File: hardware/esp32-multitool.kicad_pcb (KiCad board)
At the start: 4 copper layers, 90.4 x 58.4 mm, 68 parts, among them J1 Conn_01x03/1Wire, J2 Conn_01x04/QWiiC, J3 Conn_01x04/QWiiC, J4 Conn_01x02/VIN, J5 Conn_01x04/VIN_PROTECTED, J6 Conn_01x02/DIN, J7 Conn_01x02/AIN, J8 Conn_01x02/PWM, Q2 AO3400A, U2 mini_esp32, U3 LM393, U9 AOZ1280CI

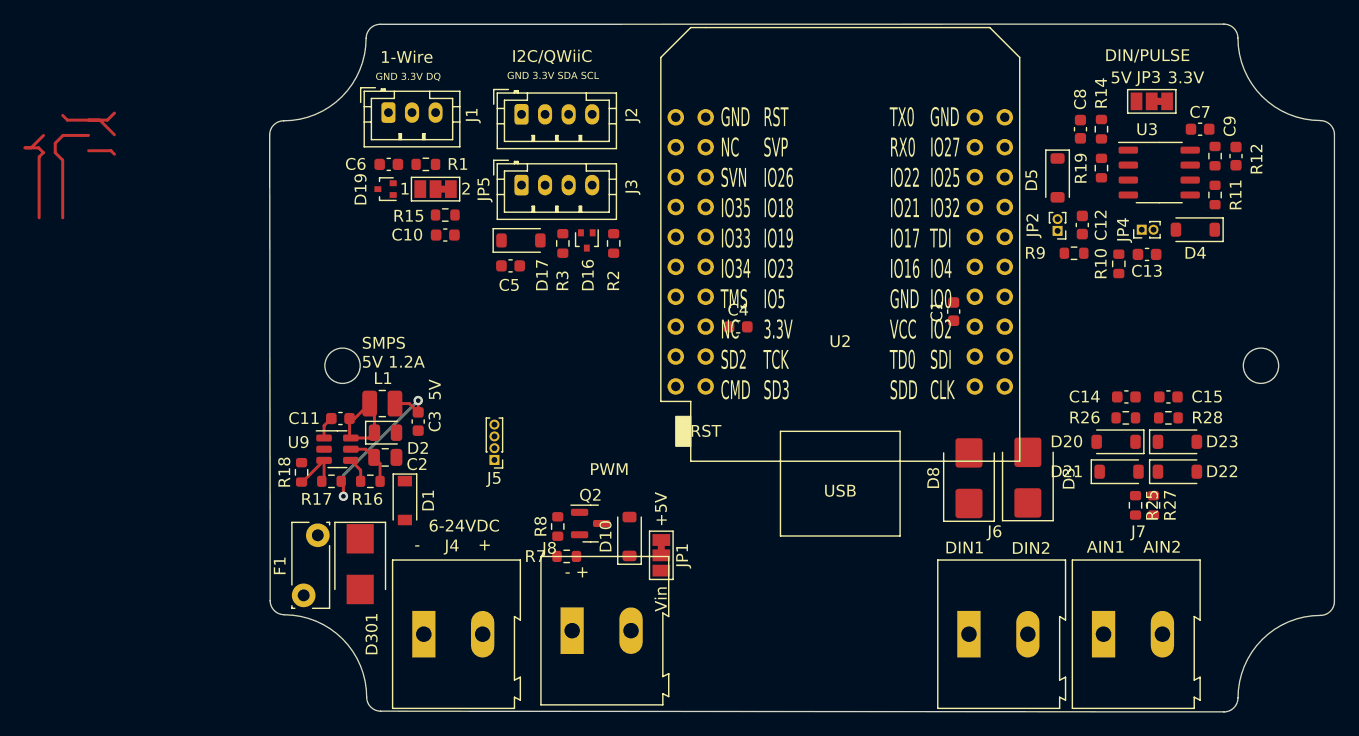
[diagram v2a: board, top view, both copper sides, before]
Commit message: Added 3D models and ran freerouting
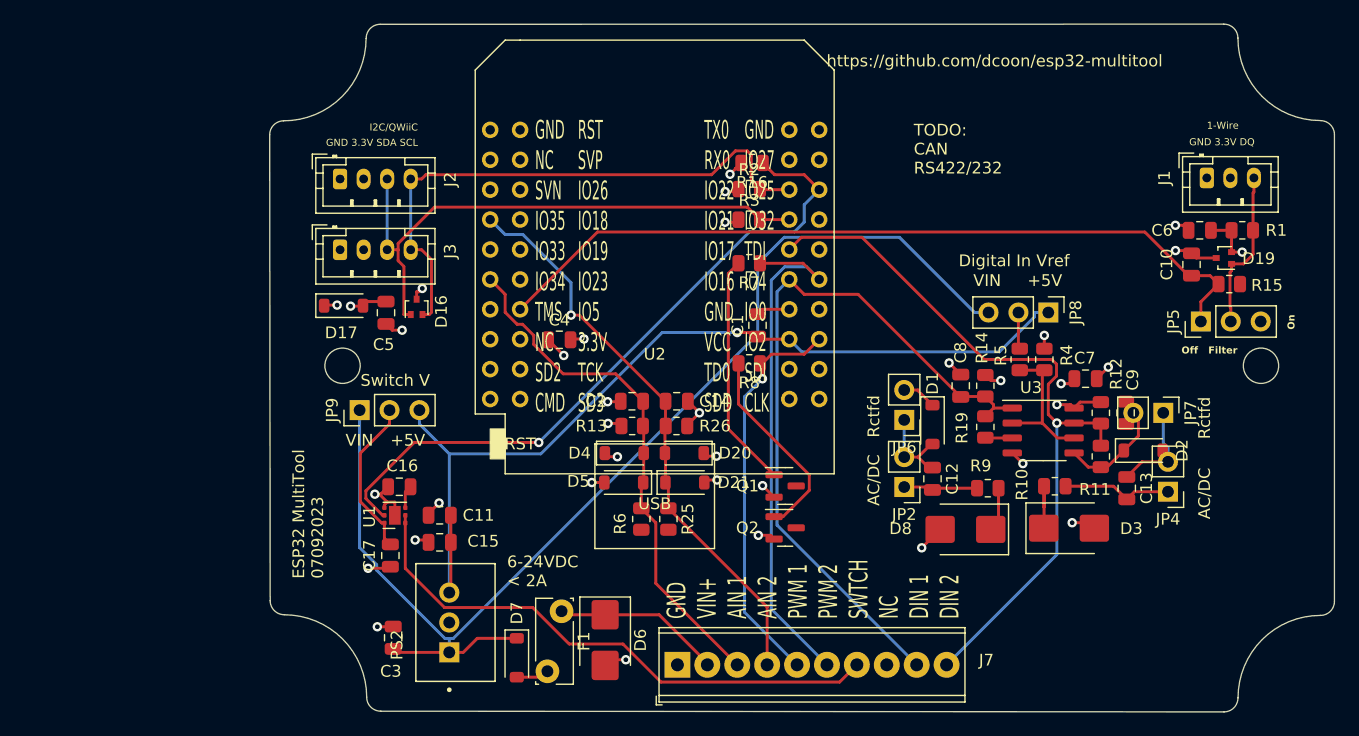
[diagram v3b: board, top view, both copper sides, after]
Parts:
- removed D10, D22, D23: D_SCHOTTKY_30V, Diode_SMD:D_SOD-123
- removed D301: D_TVS_30V, Diode_SMD:D_SMB
- removed J4: Conn_01x02/VIN, TerminalBlock:TerminalBlock_Altech_AK300-2_P5.00mm
- removed J5: Conn_01x04/VIN_PROTECTED, Connector_PinHeader_1.00mm:PinHeader_1x04_P1.00mm_Vertical
- removed J6: Conn_01x02/DIN, TerminalBlock:TerminalBlock_Altech_AK300-2_P5.00mm
- removed J8: Conn_01x02/PWM, TerminalBlock:TerminalBlock_Altech_AK300-2_P5.00mm
- removed JP1, JP3: SolderJumper_3_Bridged12, Jumper:SolderJumper-3_P1.3mm_Bridged12_Pad1.0x1.5mm_NumberLabels
- removed L1: 2.2uH, Inductor_SMD:L_1008_2520Metric
- removed R17: 49.9k, Resistor_SMD:R_0603_1608Metric
- removed R18: 9.53k, Resistor_SMD:R_0603_1608Metric
- removed R27: 100k, Resistor_SMD:R_0603_1608Metric
- removed R28: 1M, Resistor_SMD:R_0603_1608Metric
- removed U9: AOZ1280CI, Package_TO_SOT_SMD:SOT-23-6
- added C16: 4700p, Capacitor_SMD:C_0805_2012Metric, F.Cu at (99.8, 96.1)
- added C17: 4.7uF/30V, Capacitor_SMD:C_0805_2012Metric, F.Cu at (99.1, 101.9)
- added D6: D_TVS_30V, Diode_SMD:D_SMB, F.Cu at (117.3, 109.1)
- added D7: D_SCHOTTKY_30V, Diode_SMD:D_SOD-123, F.Cu at (109.8, 110.6)
- added JP6: Jumper_2_Bridged, Connector_PinHeader_2.54mm:PinHeader_1x02_P2.54mm_Vertical, F.Cu at (142.7, 90.4)
- added JP7: Jumper_2_Bridged, Connector_PinHeader_2.54mm:PinHeader_1x02_P2.54mm_Vertical, F.Cu at (164.7, 89.8)
- added JP8: Jumper_2_Open, Connector_PinHeader_2.54mm:PinHeader_1x03_P2.54mm_Vertical, F.Cu at (154.9, 81.3)
- added JP9: Jumper_3_Bridged12, Connector_PinHeader_2.54mm:PinHeader_1x03_P2.54mm_Vertical, F.Cu at (96.4, 89.6)
- added PS2: TPSM84205EAB, TPSM84205EAB:TPSM84205EAB, F.Cu at (104.1, 107.6)
- added Q1: AO3400A, Package_TO_SOT_SMD:SOT-23, F.Cu at (132.6, 96.0)
- added R13: 1M, Resistor_SMD:R_0805_2012Metric, F.Cu at (119.6, 90.9)
- added R4: 10k, Resistor_SMD:R_0805_2012Metric, F.Cu at (152.5, 85.3)
- added R5: 10k, Resistor_SMD:R_0805_2012Metric, F.Cu at (154.6, 85.3)
- added R6: 100k, Resistor_SMD:R_0805_2012Metric, F.Cu at (120.4, 98.8)
- added U1: TPS22810DRV, Package_SON:WSON-6-1EP_2x2mm_P0.65mm_EP1x1.6mm, F.Cu at (99.4, 98.5)
- C1, C10, C12, C13, C14, C4, C5, C6, C7, C8, C9: footprint Capacitor_SMD:C_0603_1608Metric -> Capacitor_SMD:C_0805_2012Metric
- C11: value 10nF -> 47uF/16V; footprint Capacitor_SMD:C_0603_1608Metric -> Capacitor_SMD:C_0805_2012Metric
- C15: value 1uF -> 47uF/16V; footprint Capacitor_SMD:C_0603_1608Metric -> Capacitor_SMD:C_0805_2012Metric
- C2: value 4.7uF/30V -> 1uF
- C3: value 10uF -> 10uF/50V; footprint Capacitor_SMD:C_0603_1608Metric -> Capacitor_SMD:C_0805_2012Metric
- D2: value D_SMPS -> D_SCHOTTKY_30V; footprint Diode_SMD:D_0805_2012Metric -> Diode_SMD:D_SOD-123
- J7: value Conn_01x02/AIN -> Conn_01x09; footprint TerminalBlock:TerminalBlock_Altech_AK300-2_P5.00mm -> TerminalBlock_Phoenix:TerminalBlock_Phoenix_MPT-0,5-10-2.54_1x10_P2.54mm_Horizontal
- JP2, JP4: footprint Connector_PinHeader_1.00mm:PinHeader_1x02_P1.00mm_Vertical -> Connector_PinHeader_2.54mm:PinHeader_1x02_P2.54mm_Vertical
- JP5: value SolderJumper_3_Bridged12 -> Jumper_3_Bridged12; footprint Jumper:SolderJumper-3_P1.3mm_Bridged12_Pad1.0x1.5mm_NumberLabels -> Connector_PinHeader_2.54mm:PinHeader_1x03_P2.54mm_Vertical
- R1, R10, R11, R12, R14, R15, R19, R2, R25, R26, R3, R8, R9: footprint Resistor_SMD:R_0603_1608Metric -> Resistor_SMD:R_0805_2012Metric
- R16: value R10k -> 10k/30V; footprint Resistor_SMD:R_0603_1608Metric -> Resistor_SMD:R_0805_2012Metric
- R7: value 10k -> 100; footprint Resistor_SMD:R_0603_1608Metric -> Resistor_SMD:R_0805_2012Metric
- U2: value mini_esp32 -> wemos_mini_esp32
- moved D19 71.4 mm to (169.8, 76.7)
- moved J1 69.7 mm to (168.4, 69.8)
- moved R1 69.6 mm to (171.4, 74.3)
- moved C6 69.1 mm to (167.8, 74.3)
- moved R15 66.8 mm to (170.3, 78.9), turned to 0 degrees
- moved JP5 66.0 mm to (167.9, 82.0), turned to 90 degrees
- moved D2 64.4 mm to (163.0, 93.0)
- moved C10 63.4 mm to (167.1, 77.2), turned to 90 degrees
- moved C15 63.1 mm to (103.2, 100.8), turned to 180 degrees
- moved D4 52.1 mm to (118.9, 93.2), turned to 0 degrees
- moved D1 45.3 mm to (145.1, 90.8)
- moved D5 45.0 mm to (118.9, 95.7), turned to 180 degrees
- moved R16 42.2 mm to (129.8, 68.6), turned to 180 degrees
- moved R25 39.7 mm to (122.7, 98.8)
- moved C14 38.2 mm to (123.4, 88.8), turned to 0 degrees
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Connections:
- net /digital_in/DIN_LINE1 renamed /DIN_LINE1
- net /digital_in/DIN_LINE2 renamed /DIN_LINE2
- C11 pad 1: /power/SMPS_BST -> +5V
- C11 pad 2: /power/SMPS_LX -> GND
- C12 pad 1: Net-(D5-A) -> Net-(D1-A)
- C13 pad 1: Net-(D4-A) -> Net-(D2-A)
- C14 pad 1: /AIN1 -> /AIN2
- C15 pad 1: /AIN2 -> +5V
- C2 pad 1: /VIN_PROTECTED -> /AIN1
- C3 pad 1: +5V -> VPP
- D1 pad 1: /VIN_PROTECTED -> Net-(D1-K)
- D2 pad 1: /power/SMPS_LX -> Net-(D2-K)
- D2 pad 2: GND -> Net-(D2-A)
- D20 pad 2: /AIN1 -> /AIN2
- D21 pad 1: /AIN1 -> /AIN2
- D4 pad 1: Net-(D4-K) -> +3.3V
- D4 pad 2: Net-(D4-A) -> /AIN1
- D5 pad 1: Net-(D5-K) -> /AIN1
- D5 pad 2: Net-(D5-A) -> GND
- F1 pad 1: /power/VIN -> /VIN
- F1 pad 2: Net-(D1-A) -> Net-(D7-A)
- J7 pad 1: /analog_in/AIN_LINE1 -> GND
- J7 pad 2: /analog_in/AIN_LINE2 -> /VIN
- JP2 pad 2: Net-(D5-A) -> Net-(D1-A)
- JP4 pad 2: Net-(D4-A) -> Net-(D2-A)
- JP5 pad 3: Net-(JP5-B) -> unconnected-(JP5-B-Pad3)
- Q2 pad 3: /pwm/PWM_NEG -> /PWM_LINE1
- R11 pad 1: Net-(D4-K) -> Net-(D2-K)
- R15 pad 2: Net-(JP5-B) -> unconnected-(R15-Pad2)
- R16 pad 1: Net-(U9-EN) -> /SWITCH1
- R16 pad 2: /VIN_PROTECTED -> GND
- R19 pad 1: Net-(D5-K) -> Net-(D1-K)
- R25 pad 1: /AIN1 -> /AIN2
- R25 pad 2: /analog_in/AIN_LINE1 -> /AIN_LINE2
- R26 pad 1: /AIN1 -> /AIN2
- R7 pad 1: GND -> /PWM2
- R7 pad 2: /PWM1 -> Net-(Q1-G)
- U2 pad 26: unconnected-(U2-IO_25-Pad26) -> /SWITCH1
- U2 pad 32: unconnected-(U2-IO_04-Pad32) -> /PWM2
- U3 pad 3: Net-(D5-K) -> Net-(D1-K)
- U3 pad 5: Net-(D4-K) -> Net-(D2-K)
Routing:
- net VPP: track 0.00 -> 101.1 mm
- net +5V: track 15.4 -> 81.2 mm, vias 2 -> 1
- net /DIN2: track 0.00 -> 63.2 mm, vias 0 -> 1
- net /DIN1: track 0.00 -> 62.7 mm
- net /1WIRE_DQ: track 7.53 -> 68.2 mm
- net /SWITCH1: track 0.00 -> 59.2 mm, vias 0 -> 1
- net /I2C_SCL: track 0.00 -> 49.2 mm
- net /AIN2: track 0.00 -> 48.9 mm, vias 0 -> 1
- net /I2C_SDA: track 0.00 -> 48.7 mm
- net /SWITCH_LINE1: track 0.00 -> 47.5 mm
- net /PWM2: track 0.00 -> 45.2 mm
- net /AIN1: track 0.00 -> 44.5 mm
- net GND: track 9.71 -> 47.8 mm, vias 0 -> 26
- net /PWM1: track 0.00 -> 34.0 mm, vias 0 -> 1
- net Net-(Q1-G): track 0.00 -> 19.9 mm
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- added copper zone on In2.Cu, net +3.3V
- added copper zone on In1.Cu, net GND
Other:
- board text added: "+5V"
- board text added: "6-24VDC < 2A"
- board text added: "AC/DC"
- board text added: "Digital In Vref"
- board text added: "ESP32 MultiTool 07092023"
- board text added: "GND VIN+ AIN 1 AIN 2 PWM 1 PWM 2 SWTCH NC DIN 1 DIN 2"
- board text added: "Off Filter"
- board text added: "On"
- board text added: "Rctfd"
- board text added: "Switch V"
- board text added: "TODO: CAN RS422/232"
- board text added: "VIN"
- board text added: "https://github.com/dcoon/esp32-multitool"
- board text removed: "+"
- board text removed: "-"
- board text removed: "- +"
- board text removed: "5V"
- board text removed: "6-24VDC"
- board text removed: "AIN1"
- board text removed: "AIN2"
- board text removed: "DIN/PULSE"
- board text removed: "DIN1"
- board text removed: "DIN2"
- board text removed: "PWM"
- board text removed: "SMPS 5V 1.2A"
